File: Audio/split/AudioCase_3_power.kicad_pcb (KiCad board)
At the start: 2 copper layers, 55.3 x 44 mm, 15 parts, among them J4 PWR_IN, J5 PWR_OUT, U1 MCW03

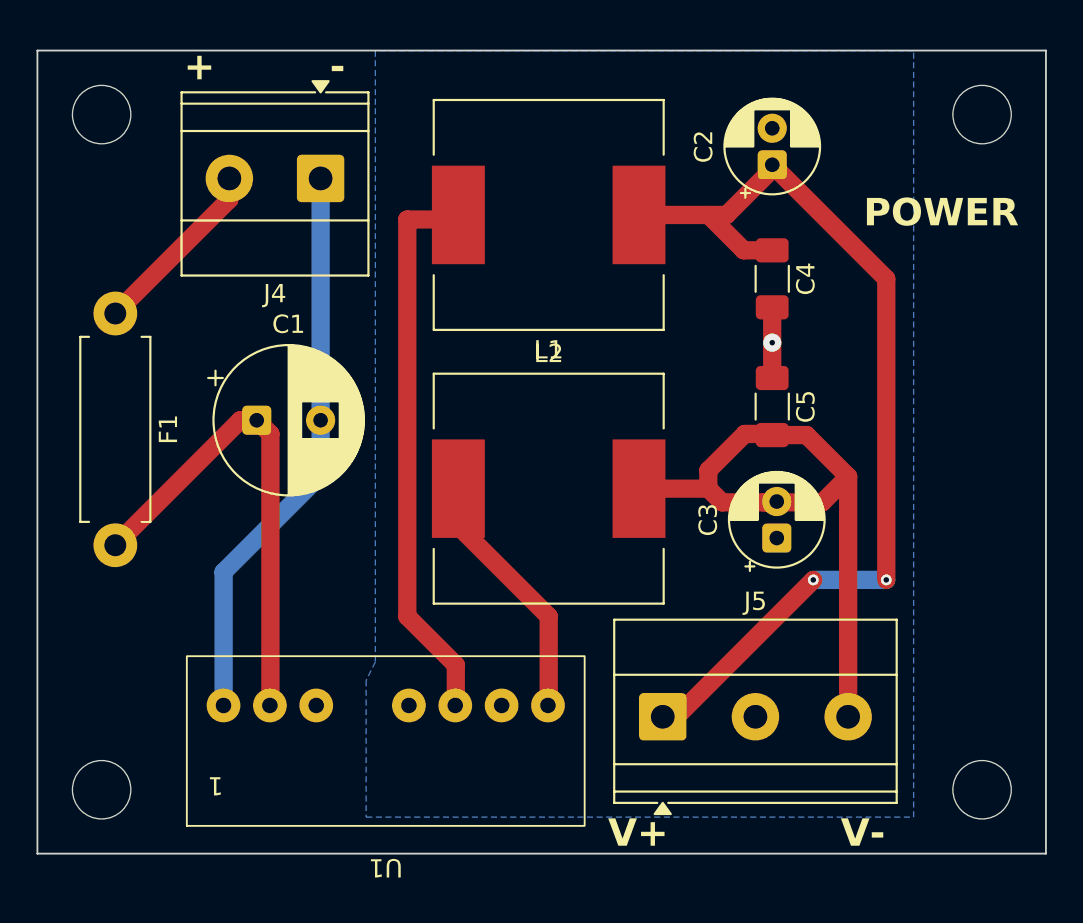
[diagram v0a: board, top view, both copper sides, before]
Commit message: ノイズ対策と製造データ整備: デカップリング追加・GNDベタ強化・シルク整理
- 5V_+ラインにデカップリング/バルク(C34-C37)を追加し、リレー切替時の電源変動を抑制
- F.CuにCTRL_GND/GNDベタを追加し、ステッチングビアで表裏GNDを補強(DC-DC周辺含む)
- 端子台ラベル等のシルク重なりを解消(J11/J14/J6/J4/L1/L2ほか)
- masterから4基板を再split、Gerber/zipを再生成

Co-authored-by: Cursor <cursoragent@cursor.com>
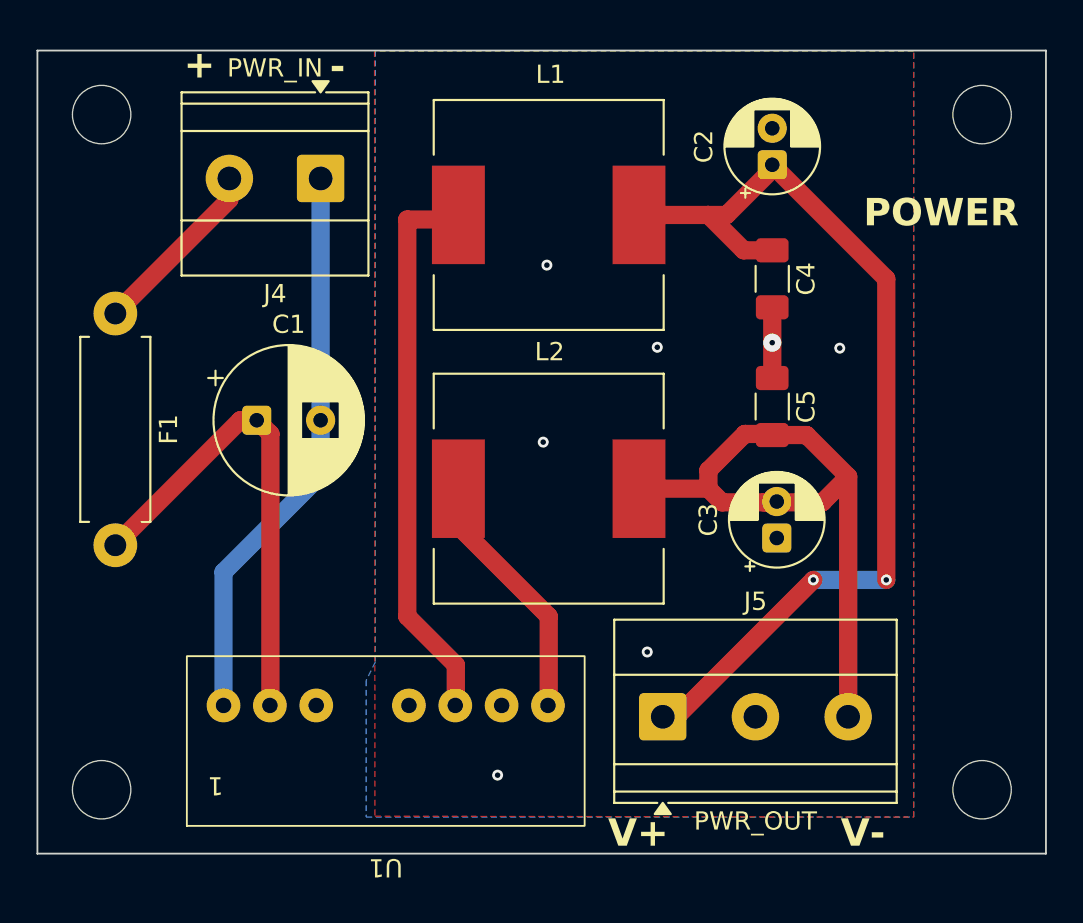
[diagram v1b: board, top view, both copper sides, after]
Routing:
- net GND: vias 1 -> 7
- added copper zone on F.Cu, net GND

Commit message: AudioCaseのリレー・EQネット整理と分割Gerberを再生成する。
Controllでアンプ別リレーネットを分離し、EQのバッファ入力をL/R_BUFF_INに改名。4枚分割PCBと発注用Gerberを更新し、RVパネルKiKit矩形とmacOS向けツール探索も修正。

Co-authored-by: Cursor <cursoragent@cursor.com>
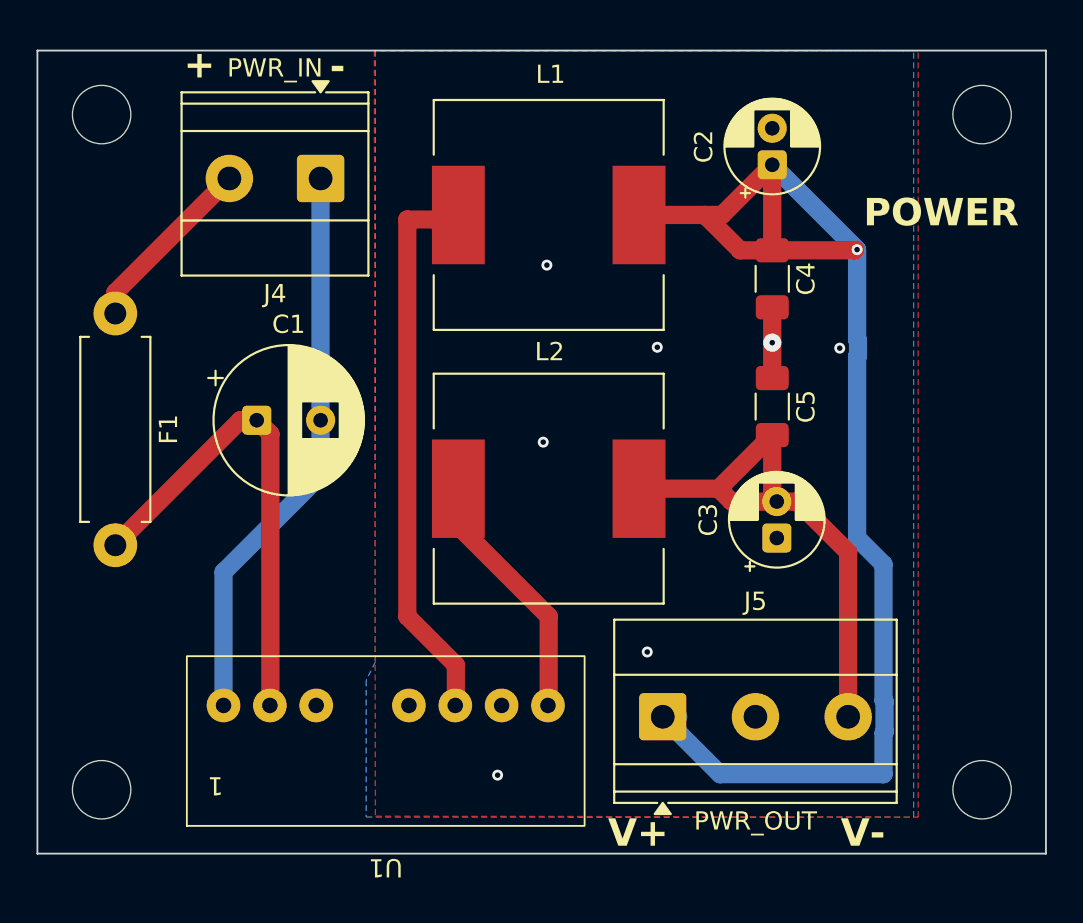
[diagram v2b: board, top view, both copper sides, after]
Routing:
- net /Controll/AMP_V+_IN: track 53.6 -> 72.5 mm, vias 2 -> 1
- net /Controll/AMP_V-_IN: track 36.4 -> 29.8 mm

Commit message: 分割Gerberを再生成し、05のzip名をスクリプト表記に揃える。
初号向け再出力を取り込み、旧05_rv_conv.zipを05_rv_convert.zipへ置き換える。

Co-authored-by: Cursor <cursoragent@cursor.com>
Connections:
- net /Controll/PD_GND_IN renamed /MeasurementADC/ADC_GND_IN
